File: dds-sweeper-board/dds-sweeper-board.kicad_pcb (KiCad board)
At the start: 2 copper layers, 53 x 65 mm, 12 parts, among them J1 REF CLK OUT, J3 1V8, J4 AD9959 Eval Header, J5 Trigger In, J6 RESET, J7 DDS PWR, U1 Pico, U3 XC6210B18

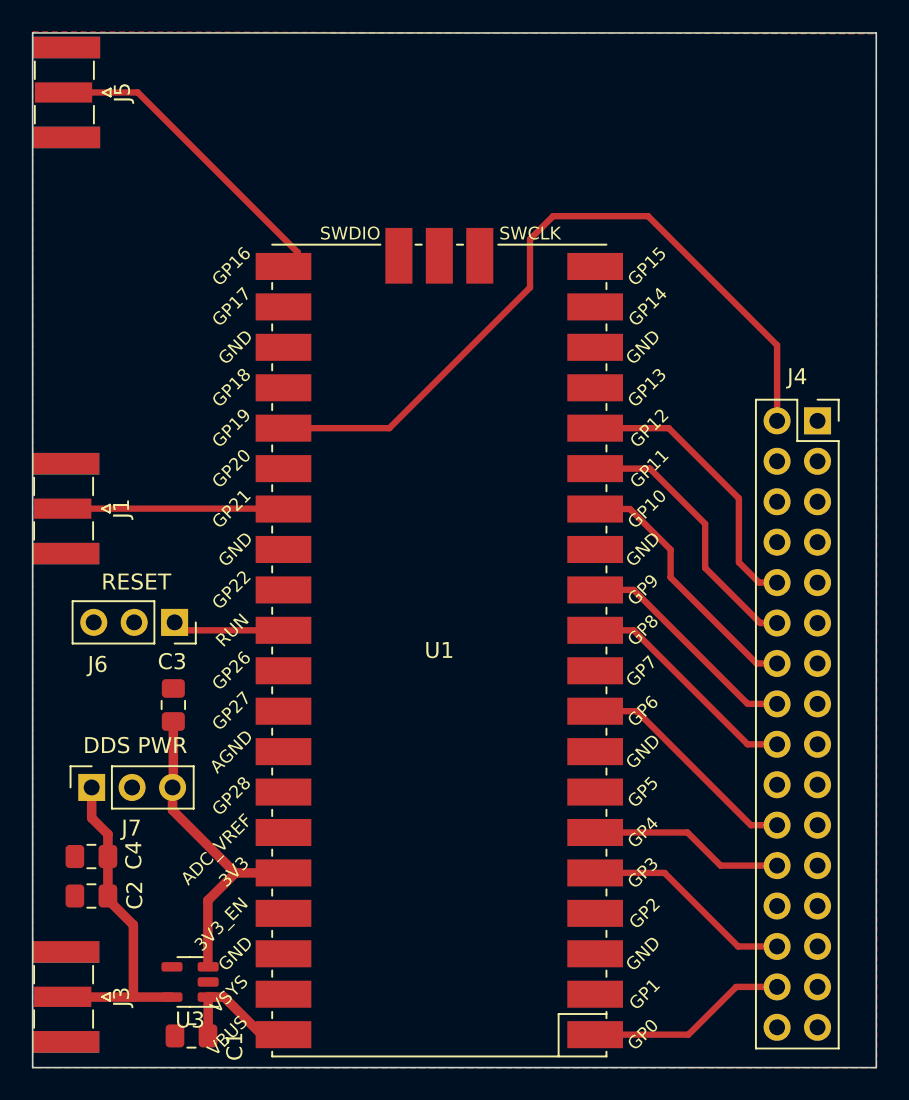
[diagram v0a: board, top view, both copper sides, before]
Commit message: Update breakout board to have an input buffer on the trigger line.
Should help with longer cable runs on the trigger input.
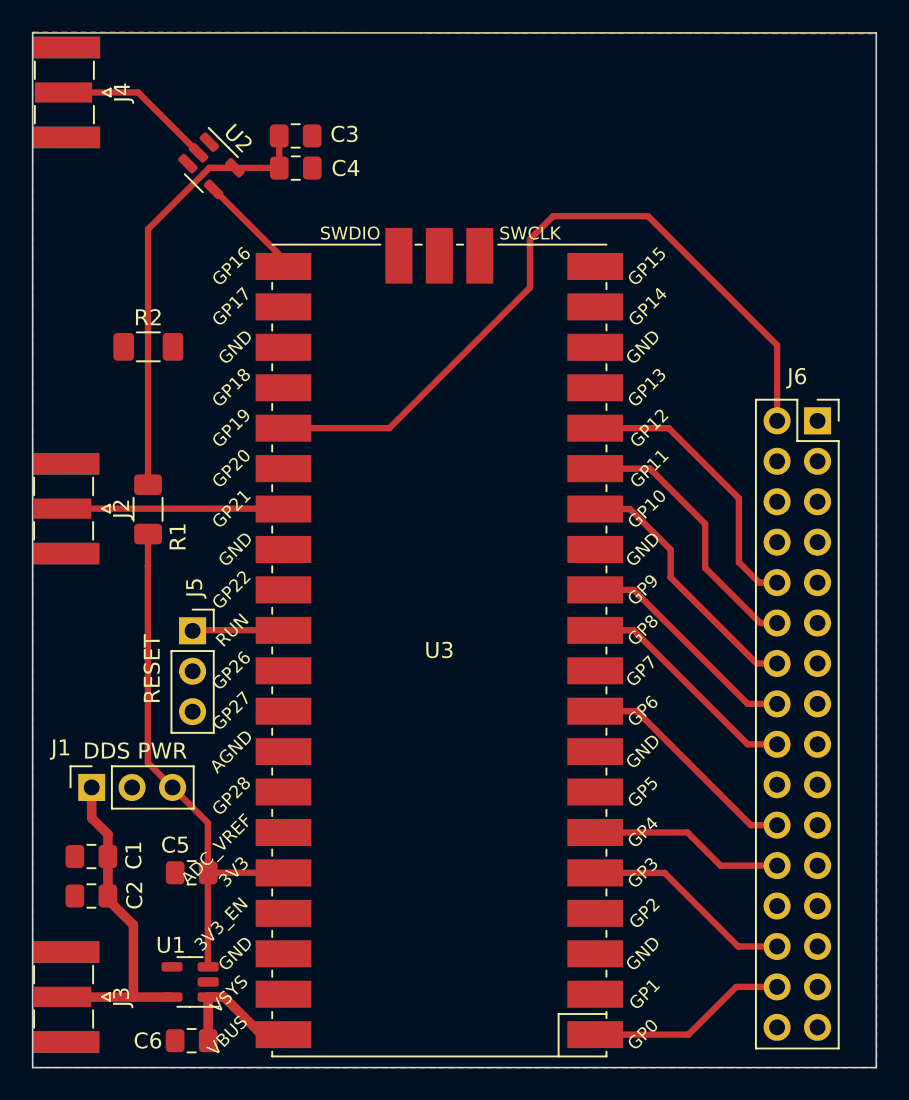
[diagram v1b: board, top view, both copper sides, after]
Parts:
- removed the C1 at (42.0, 97.0)
- added C4: 0.1uF, Capacitor_SMD:C_0805_2012Metric_Pad1.18x1.45mm_HandSolder, F.Cu at (48.5, 42.5)
- added C5: 0.1uF, Capacitor_SMD:C_0805_2012Metric_Pad1.18x1.45mm_HandSolder, F.Cu at (42.0, 86.8)
- added C6: 0.1uF, Capacitor_SMD:C_0805_2012Metric_Pad1.18x1.45mm_HandSolder, F.Cu at (42.0, 97.3)
- added R1: 0, Resistor_SMD:R_1206_3216Metric_Pad1.30x1.75mm_HandSolder, F.Cu at (39.2, 63.9)
- added R2: 0, Resistor_SMD:R_1206_3216Metric_Pad1.30x1.75mm_HandSolder, F.Cu at (39.3, 53.7)
- added U2: 74LVC1G17, Package_TO_SOT_SMD:SOT-23-5, F.Cu at (43.2, 42.3)
- C3: value 0.1uF -> 1uF
- moved C3 36.6 mm to (48.5, 40.5), turned to 0 degrees
- moved J5 1.25 mm to (42.0, 71.6), turned to 0 degrees
- renumbered C4 to C1, J7 to J1, J1 to J2, J5 to J4, J6 to J5, J4 to J6, U3 to U1, U1 to U3
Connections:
- C3 pad 1: GND -> Net-(U2-VCC)
- C3 pad 2: 3V3 -> GND
- J4 pad 1: /TRIG_IN -> Net-(J4-In)
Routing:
- net Net-(U2-VCC): track 0.00 -> 28.1 mm
- net 3V3: track 21.7 -> 34.4 mm
- net /TRIG_IN: track 19.6 -> 7.31 mm
- net Net-(J4-In): track 0.00 -> 9.85 mm
- net Net-(J5-Pin_1): track 8.34 -> 6.63 mm

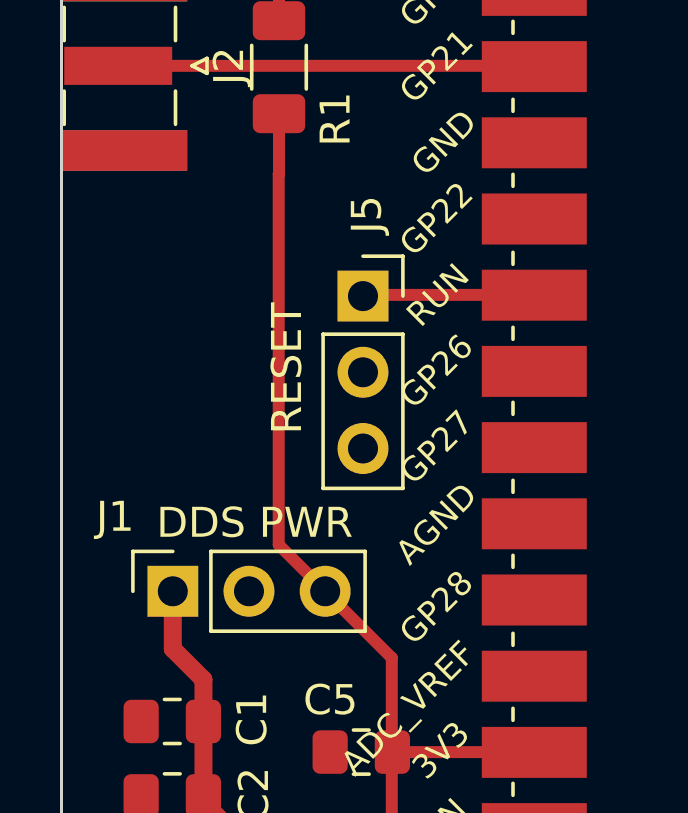
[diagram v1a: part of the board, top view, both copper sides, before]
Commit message: Update KiCAD project with proper header footprint (instead of sockets) and add 3D components so 3D board render is correct.
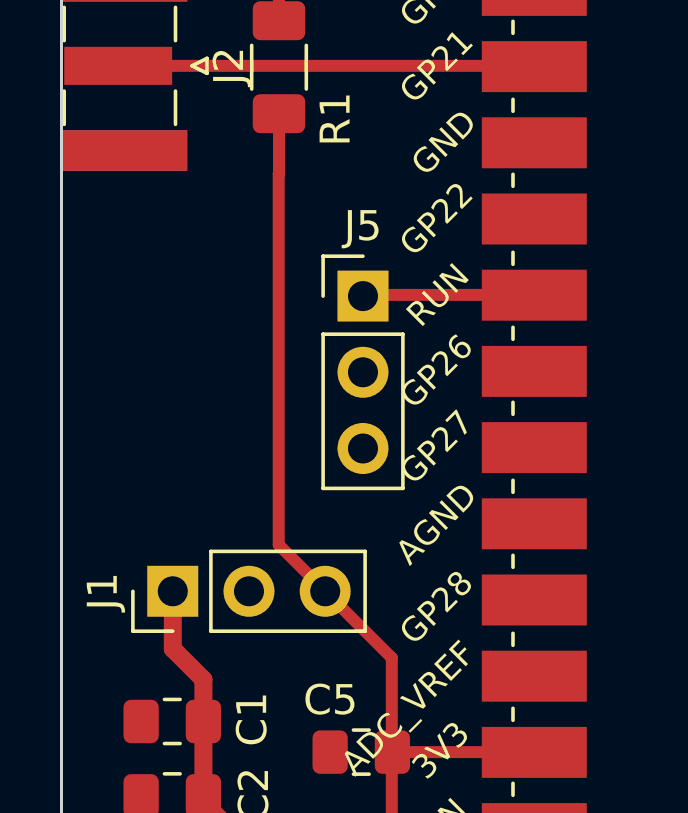
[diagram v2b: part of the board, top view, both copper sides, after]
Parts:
- J1, J5: footprint Connector_PinSocket_2.54mm:PinSocket_1x03_P2.54mm_Vertical -> Connector_PinHeader_2.54mm:PinHeader_1x03_P2.54mm_Vertical
